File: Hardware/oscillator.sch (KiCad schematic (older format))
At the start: 3 parts, among them U5 SIT2001BI-S2-33S-100.000000D

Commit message: Complete new schematic
Added MAX232 and fixed test points on switches
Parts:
- TP10: footprint TestPoint:TestPoint_Pad_1.0x1.0mm -> TestPoint:TestPoint_THTPad_1.0x1.0mm_Drill0.5mm
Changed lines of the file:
@@
 F 0 "TP10" H 6858 4018 50  0000 L CNN
 F 1 "TestPoint" H 6858 3927 50  0000 L CNN
-F 2 "TestPoint:TestPoint_Pad_1.0x1.0mm" H 7000 3900 50  0001 C CNN
+F 2 "TestPoint:TestPoint_THTPad_1.0x1.0mm_Drill0.5mm" H 7000 3900 50  0001 C CNN
 F 3 "~" H 7000 3900 50  0001 C CNN
 	1    6800 3900

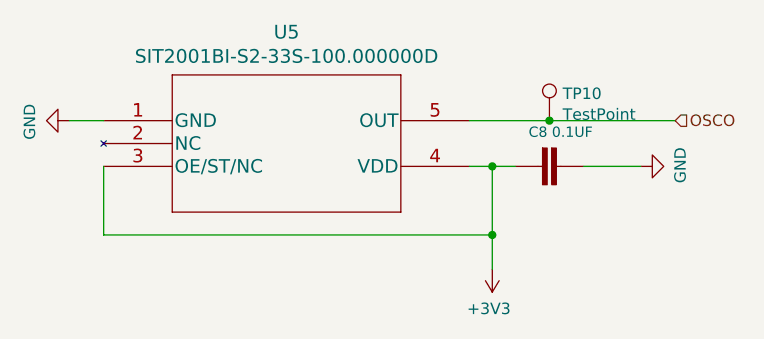
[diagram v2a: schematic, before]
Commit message: Fix incorrect footprints
Fixed incorrect footprint for IRLML2060 and updated LED values to use CLVBA-FKA.
Also started deleting unneccessary test points
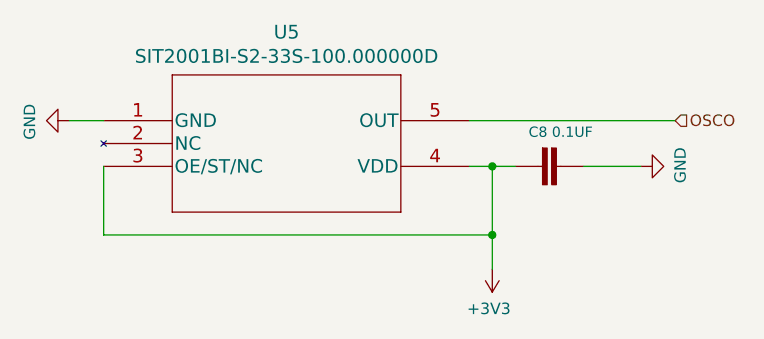
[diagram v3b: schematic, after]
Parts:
- removed TP10: TestPoint, TestPoint:TestPoint_THTPad_1.0x1.0mm_Drill0.5mm, symbol Connector:TestPoint
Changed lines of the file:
@@
 	4850 4400 4850 4100
 Wire Wire Line
-	6450 3900 6800 3900
-Wire Wire Line
 	6450 4100 6550 4100
-$Comp
-L Connector:TestPoint TP?
-U 1 1 5F68C85F
-P 6800 3900
-AR Path="/5F68C85F" Ref="TP?"  Part="1"
-AR Path="/5F66C553/5F68C85F" Ref="TP10"  Part="1"
-F 0 "TP10" H 6858 4018 50  0000 L CNN
-F 1 "TestPoint" H 6858 3927 50  0000 L CNN
-F 2 "TestPoint:TestPoint_THTPad_1.0x1.0mm_Drill0.5mm" H 7000 3900 50  0001 C CNN
-F 3 "~" H 7000 3900 50  0001 C CNN
-	1    6800 3900
-	1    0    0    -1
-$EndComp
 $Comp
 L power:GND #PWR?
@@
 	0    1    1    0
 $EndComp
-Connection ~ 6800 3900
-Wire Wire Line
-	6800 3900 7350 3900
 Text HLabel 7350 3900 2    50   Input ~ 0
 OSCO
+Wire Wire Line
+	6450 3900 7350 3900
 $EndSCHEMATC

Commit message: Fix faulty debounce circuit
Used wrong value resistor/misplaced on each switch.
Also adjusted value of RC circuits for a time constant of 1 microsecond (was 1 millisecond before)
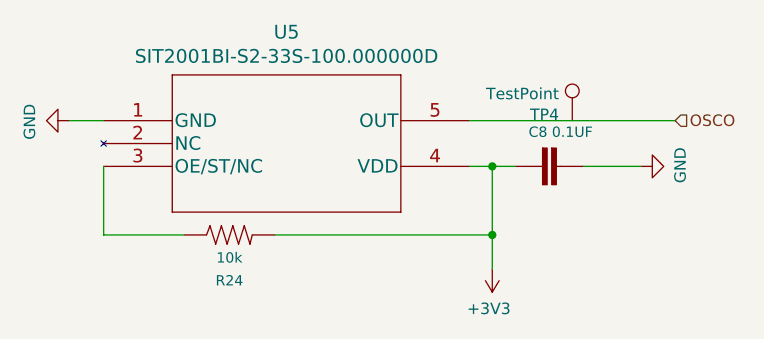
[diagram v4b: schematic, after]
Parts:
- added R24: 10k, Resistor_SMD:R_0603_1608Metric_Pad1.05x0.95mm_HandSolder, symbol serial-mini:Resistor
- added TP4: TestPoint, TestPoint:TestPoint_Pad_1.0x1.0mm, symbol Connector:TestPoint
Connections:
- net +3V3: now also R24.2; no longer U5.3 (OE/ST/NC)
- new net: R24.1, U5.3 (OE/ST/NC)
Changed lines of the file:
@@
 Wire Wire Line
 	6950 4100 7200 4100
-Wire Wire Line
-	6550 4100 6550 4400
 $Comp
 L power:+3V3 #PWR?
@@
 	-1   0    0    1
 $EndComp
-Wire Wire Line
-	4850 4400 6550 4400
-Connection ~ 6550 4400
-Wire Wire Line
-	6550 4400 6550 4550
 Wire Wire Line
 	4700 3900 4850 3900
@@
 Wire Wire Line
 	6450 3900 7350 3900
+$Comp
+L serial-mini:Resistor R24
+U 1 1 5F351CC1
+P 5400 4400
+F 0 "R24" H 5400 4200 45  0000 C CNN
+F 1 "10k" H 5400 4300 45  0000 C CNN
+F 2 "Resistor_SMD:R_0603_1608Metric_Pad1.05x0.95mm_HandSolder" H 5400 4550 20  0001 C CNN
+F 3 "" H 5400 4400 60  0001 C CNN
+F 4 " " H 5400 4521 60  0000 C CNN "Field4"
+	1    5400 4400
+	1    0    0    -1
+$EndComp
+Wire Wire Line
+	6550 4100 6550 4400
+Wire Wire Line
+	4850 4400 5200 4400
+Wire Wire Line
+	5600 4400 6550 4400
+Connection ~ 6550 4400
+Wire Wire Line
+	6550 4400 6550 4550
+$Comp
+L Connector:TestPoint TP?
+U 1 1 5F358C4F
+P 6900 3900
+AR Path="/5F358C4F" Ref="TP?"  Part="1"
+AR Path="/5F66C553/5F358C4F" Ref="TP4"  Part="1"
+F 0 "TP4" H 6842 3926 50  0000 R CNN
+F 1 "TestPoint" H 6842 4017 50  0000 R CNN
+F 2 "TestPoint:TestPoint_Pad_1.0x1.0mm" H 7100 3900 50  0001 C CNN
+F 3 "~" H 7100 3900 50  0001 C CNN
+	1    6900 3900
+	1    0    0    -1
+$EndComp
 $EndSCHEMATC

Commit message: Fix weird routing
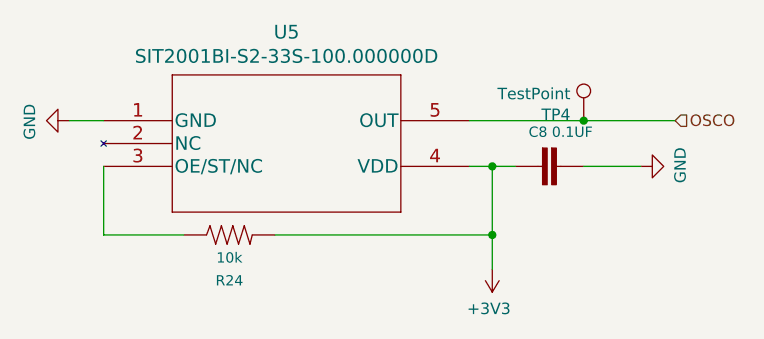
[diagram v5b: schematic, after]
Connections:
- net OSCO: now also TP4.1
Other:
- moved on the sheet: TP4
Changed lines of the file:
@@
 OSCO
 Wire Wire Line
-	6450 3900 7350 3900
+	6450 3900 6950 3900
 $Comp
 L serial-mini:Resistor R24
@@
 L Connector:TestPoint TP?
 U 1 1 5F358C4F
-P 6900 3900
+P 6950 3900
 AR Path="/5F358C4F" Ref="TP?"  Part="1"
 AR Path="/5F66C553/5F358C4F" Ref="TP4"  Part="1"
-F 0 "TP4" H 6842 3926 50  0000 R CNN
-F 1 "TestPoint" H 6842 4017 50  0000 R CNN
-F 2 "TestPoint:TestPoint_Pad_1.0x1.0mm" H 7100 3900 50  0001 C CNN
-F 3 "~" H 7100 3900 50  0001 C CNN
-	1    6900 3900
+F 0 "TP4" H 6892 3926 50  0000 R CNN
+F 1 "TestPoint" H 6892 4017 50  0000 R CNN
+F 2 "TestPoint:TestPoint_Pad_1.0x1.0mm" H 7150 3900 50  0001 C CNN
+F 3 "~" H 7150 3900 50  0001 C CNN
+	1    6950 3900
 	1    0    0    -1
 $EndComp
+Connection ~ 6950 3900
+Wire Wire Line
+	6950 3900 7350 3900
 $EndSCHEMATC
